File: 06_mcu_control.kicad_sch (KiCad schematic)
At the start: 13 parts, among them J6 Cortex Debug 10-pin, J7 Debug breakout (SWDIO,SWCLK,N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, U7 STM32G031K8T6

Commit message: Root sheet + full-hierarchy fixes (PWR_FLAG uniqueness, annotation, D-designator collision)
- red-light-panel.kicad_sch: 7 sheet symbols, no sheet-pins (global-label
  connectivity throughout, see docs/design_notes.md).
- tools/kicad_gen/fix_instance_paths.py: one-time pass populating each
  sub-sheet's per-symbol instances block with the real root-relative path
  (kicad-cli sch upgrade was silently emptying these -- invisible to ERC,
  but kicad-cli sch export bom flagged it as an annotation error).
- Fixed: multiple PWR_FLAGs on the same merged net conflicting with each
  other at full-hierarchy scale (now exactly one per net, project-wide);
  duplicate unnumbered '#FLG' references across sheets; a real
  reference-designator collision in the original BOM itself (D5-D68 LED
  range numerically includes D6/D7/D8, reused for sheet 6/7 parts --
  renumbered those three to D69/D70/D71).

Full-hierarchy 'kicad-cli sch erc' on the root sheet: 0 errors (157
cosmetic endpoint-off-grid warnings, 3 expected lib_symbol_mismatch
warnings from flattened extends-based parts). 'kicad-cli sch export bom':
153 rows, zero blank footprints, zero duplicate references, no
annotation warning.

Co-Authored-By: Claude Sonnet 5 <noreply@anthropic.com>
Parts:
- removed D6, D7: TPD4E001DBVR (corrected from BOM's TPD4E001DZDR -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, Package_TO_SOT_SMD:SOT-23-6, symbol red-light-panel:TPD4E001DBVR
- added D69, D70: TPD4E001DBVR (corrected from BOM's TPD4E001DZDR -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, Package_TO_SOT_SMD:SOT-23-6, symbol red-light-panel:TPD4E001DBVR
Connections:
- net 3V3: now also D69.6 (VCC), D70.6 (VCC)
- net BTN_DIMM: now also D69.4 (IO3)
- net BTN_DIMP: now also D69.3 (IO2)
- net BTN_MODE: now also D69.5 (IO4)
- net BTN_PWR: now also D69.1 (IO1)
- net GND: now also D69.2 (GND), D70.2 (GND)
- net NRST: now also D70.4 (IO3)
- net SWCLK: now also D70.3 (IO2)
- net SWDIO: now also D70.1 (IO1)

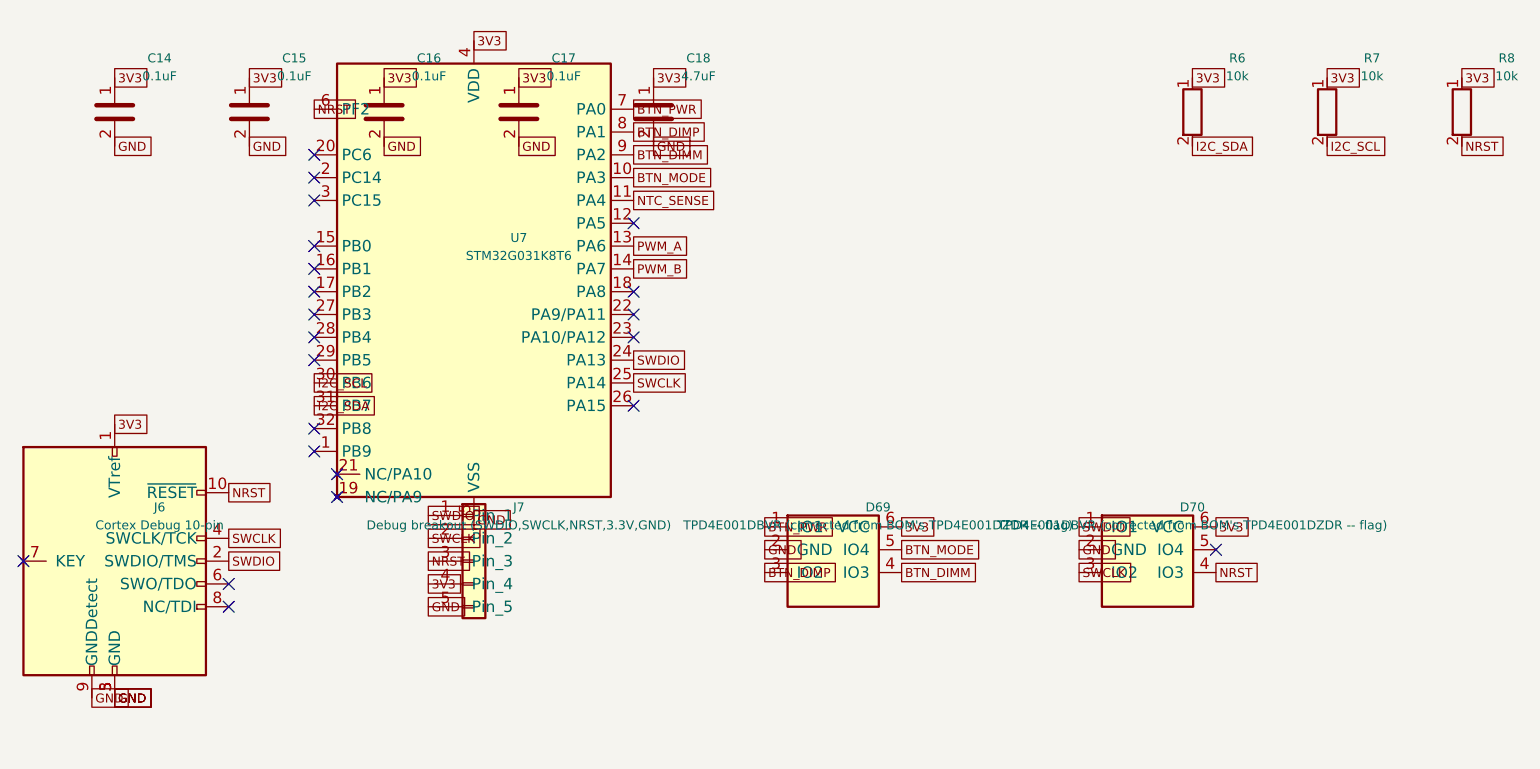
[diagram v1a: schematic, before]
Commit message: Schematic: replace global-label power nets with real power symbols
GND, VBAT, VBAT_PROT, 3V3, and USB_VBUS now get an actual KiCad power
symbol at every pin (power:GND, power:+3V3 with Value overridden to
'3V3', power:VBUS overridden to 'USB_VBUS', and two custom symbols for
VBAT/VBAT_PROT copied from stock power:+BATT into
libs/red-light-panel.kicad_sym) instead of a plain GlobalLabel -- the
idiomatic convention for power rails. All other cross-sheet signal nets
(I2C, PWM, LED channel outputs, etc.) remain GlobalLabels, which still
makes sense for data/PWM signals.

Confirmed empirically before rolling this out: overriding a stock power
symbol's Value does change its effective net name (power:+3V3 with
Value='3V3' correctly nets as '3V3'), and every power symbol's pin is
still power_in (never power_out), so existing PWR_FLAG placements are
unaffected. 0 ERC errors after the change; BOM still 153 components /
48 grouped rows, zero blank footprints, zero duplicate references.

Co-Authored-By: Claude Sonnet 5 <noreply@anthropic.com>
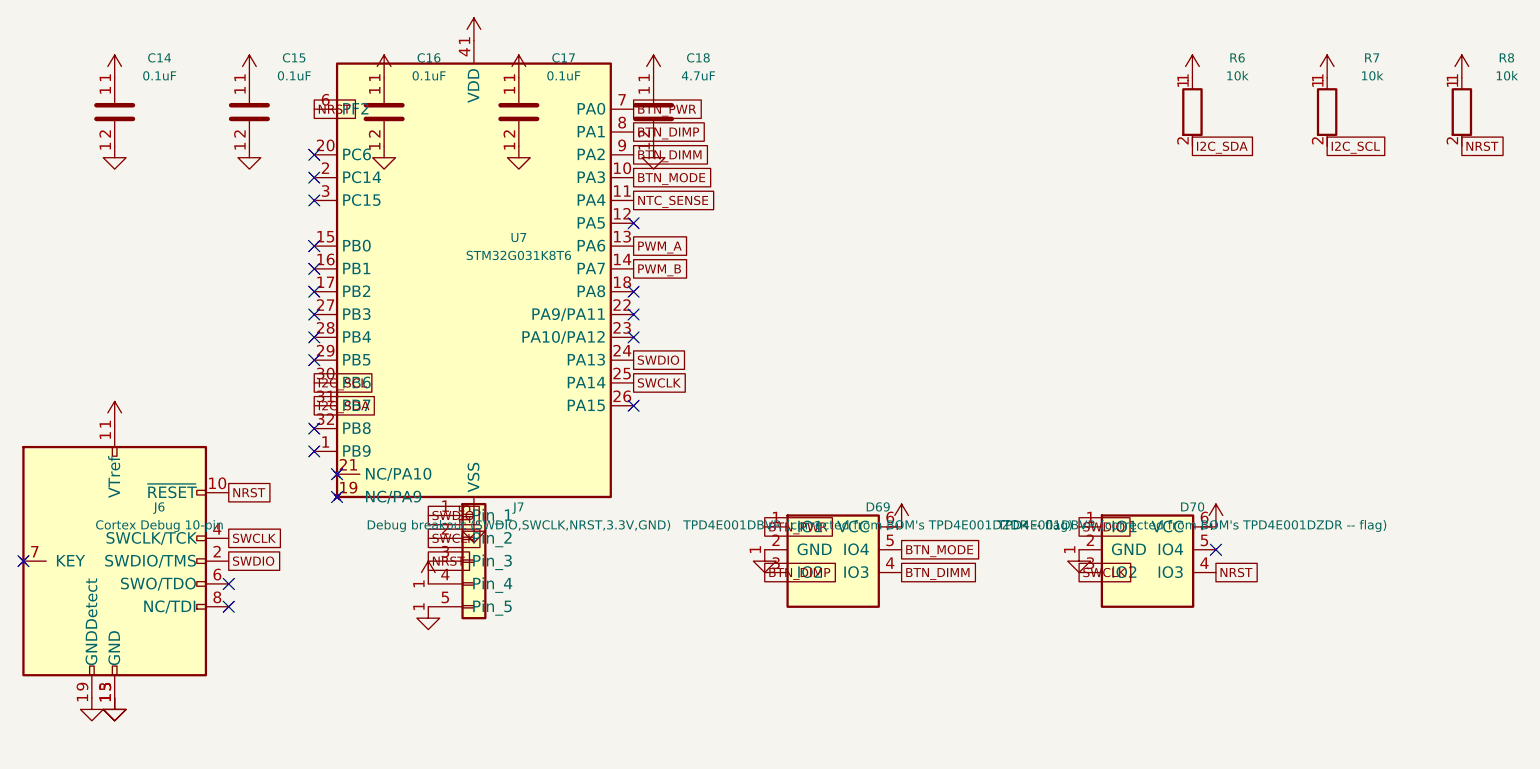
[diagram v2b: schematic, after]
